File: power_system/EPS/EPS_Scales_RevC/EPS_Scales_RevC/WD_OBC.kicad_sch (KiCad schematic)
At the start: 38 parts, among them J18 Conn_01x04, J19 Conn_01x04, U14 TLV1704

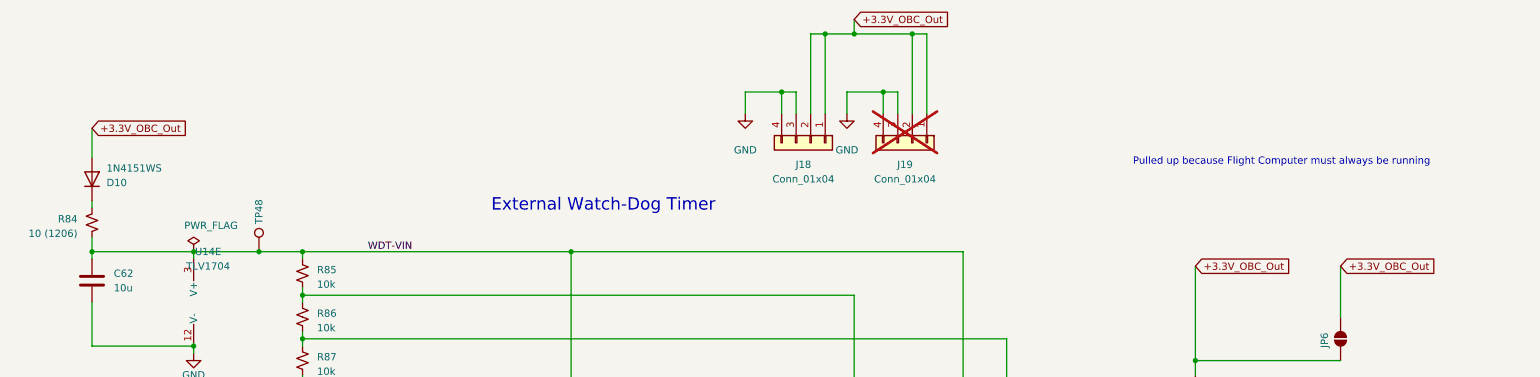
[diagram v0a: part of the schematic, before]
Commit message: Schematic and Layout changes
Made all watch dogs powered by +5v perif supply
All INAs are now powered by the 3.3v OBC supply.
DFU 16 connectors were updated to through hole versions.
Redundant test points were removed.
Layout needs work to reroute new items.
Still need to add I2C buffer
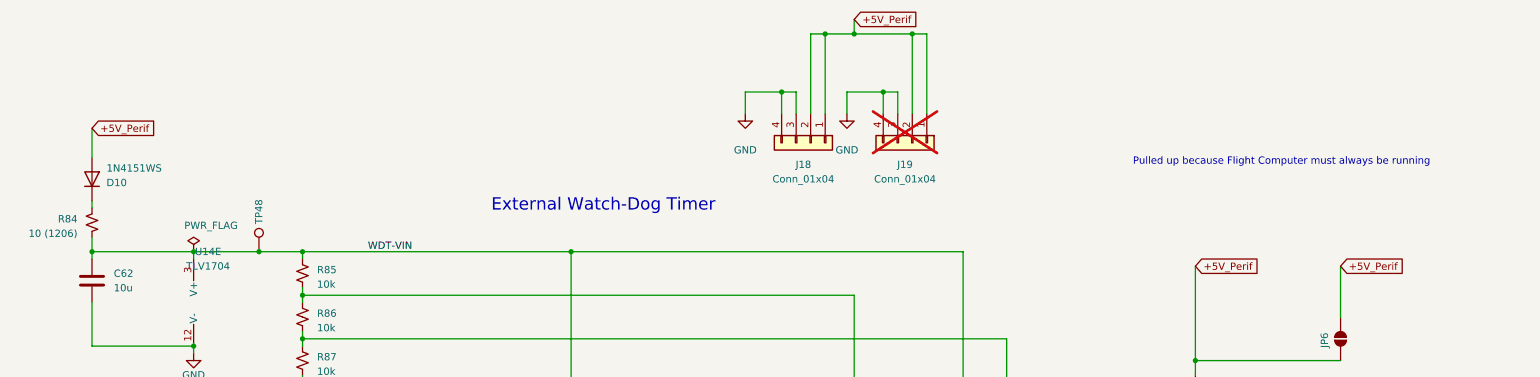
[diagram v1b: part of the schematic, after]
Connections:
- net +3.3V_OBC_Out renamed +5V_Perif
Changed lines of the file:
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@@
-		)
-	)
-	(global_label "+3.3V_OBC_Out"
-		(shape input)
-		(at 163.83 15.24 0)
-		(fields_autoplaced yes)
-		(effects
-			(font
-				(size 1.27 1.27)
-			)
-			(justify left)
-		)
-		(property "Intersheetrefs" "${INTERSHEET_REFS}"
-			(at 181.5109 15.24 0)
-			(effects
-				(font
-					(size 1.27 1.27)
-				)
-				(justify left)
-				(hide yes)
-			)
-		)
-	)
-	(global_label "+3.3V_OBC_Out"
-		(shape input)
-		(at 30.48 34.29 0)
-		(fields_autoplaced yes)
-		(effects
-			(font
-				(size 1.27 1.27)
-			)
-			(justify left)
-		)
-		(property "Intersheetrefs" "${INTERSHEET_REFS}"
-			(at 48.1609 34.29 0)
-			(effects
-				(font
-					(size 1.27 1.27)
-				)
-				(justify left)
-				(hide yes)
-			)
 		)
 	)
@@
 		)
 	)
-	(global_label "+3.3V_OBC_Out"
+	(global_label "+5V_Perif"
+		(shape input)
+		(at 163.83 15.24 0)
+		(fields_autoplaced yes)
+		(effects
+			(font
+				(size 1.27 1.27)
+			)
+			(justify left)
+		)
+		(property "Intersheetrefs" "${INTERSHEET_REFS}"
+			(at 176.1286 15.24 0)
+			(effects
+				(font
+					(size 1.27 1.27)
+				)
+				(justify left)
+				(hide yes)
+			)
+		)
+	)
+	(global_label "+5V_Perif"
 		(shape input)
 		(at 223.52 58.42 0)
@@
 		)
 		(property "Intersheetrefs" "${INTERSHEET_REFS}"
-			(at 241.2009 58.42 0)
-			(effects
-				(font
-					(size 1.27 1.27)
-				)
-				(justify left)
-				(hide yes)
-			)
-		)
-	)
-	(global_label "+3.3V_OBC_Out"
-		(shape input)
-		(at 248.92 58.42 0)
-		(fields_autoplaced yes)
-		(effects
-			(font
-				(size 1.27 1.27)
-			)
-			(justify left)
-		)
-		(property "Intersheetrefs" "${INTERSHEET_REFS}"
-			(at 266.6009 58.42 0)
+			(at 235.8186 58.42 0)
 			(effects
 				(font
@@
 				(hide yes)
 			)
+		)
+	)
+	(global_label "+5V_Perif"
+		(shape input)
+		(at 30.48 34.29 0)
+		(fields_autoplaced yes)
+		(effects
+			(font
+				(size 1.27 1.27)
+			)
+			(justify left)
+		)
+		(property "Intersheetrefs" "${INTERSHEET_REFS}"
+			(at 42.7786 34.29 0)
+			(effects
+				(font
+					(size 1.27 1.27)
+				)
+				(justify left)
+				(hide yes)
+			)
+		)
+	)
+	(global_label "+5V_Perif"
+		(shape input)
+		(at 248.92 58.42 0)
+		(fields_autoplaced yes)
+		(effects
+			(font
+				(size 1.27 1.27)
+			)
+			(justify left)
+		)
+		(property "Intersheetrefs" "${INTERSHEET_REFS}"
+			(at 261.2186 58.42 0)
+			(effects
+				(font
+					(size 1.27 1.27)
+				)
+				(justify left)
+				(hide yes)
+			)

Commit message: Schematic Revisions
Added updated block diagram
Added Individual watch dog setups for each subsystem. Resistor and Capacitor values must be modified to reflect desired time range.
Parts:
- removed J19: Conn_01x04, Connector_PinSocket_2.54mm:PinSocket_1x04_P2.54mm_Vertical, symbol Connector_Generic:Conn_01x04
- removed JP6: SolderJumper_2_Open, Jumper:SolderJumper-2_P1.3mm_Open_RoundedPad1.0x1.5mm, symbol Jumper:SolderJumper_2_Open
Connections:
- net +5V_Perif renamed +3.3V_OBC

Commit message: Layout Complete
Added I2C buffer
Found replacement inductor for 10uH
Added footprints for new components
Last thing missing is changing the solder mask sizing on most footprints to remove the errors.
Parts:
- D10, D12: footprint Diode_SMD:D_SOD-323 -> RevC Footprints:SODFL2512X100N
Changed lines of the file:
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@@
 			)
 		)
-		(property "Footprint" "Diode_SMD:D_SOD-323"
+		(property "Footprint" "RevC Footprints:SODFL2512X100N"
 			(at 177.8 137.16 0)
 			(effects
@@
 			)
 		)
-		(property "Footprint" "Diode_SMD:D_SOD-323"
+		(property "Footprint" "RevC Footprints:SODFL2512X100N"
 			(at 30.48 43.18 0)
 			(effects

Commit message: Revert "Luca branch v2"
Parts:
- added J19: Conn_01x04, Connector_PinSocket_2.54mm:PinSocket_1x04_P2.54mm_Vertical, symbol Connector_Generic:Conn_01x04
- added JP6: SolderJumper_2_Open, Jumper:SolderJumper-2_P1.3mm_Open_RoundedPad1.0x1.5mm, symbol Jumper:SolderJumper_2_Open
- D10, D12: footprint RevC Footprints:SODFL2512X100N -> Diode_SMD:D_SOD-323
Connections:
- net GND: now also J19.3 (Pin_3), J19.4 (Pin_4)
- net +3.3V_OBC renamed +5V_Perif
- net +5V_Perif: now also J19.1 (Pin_1), J19.2 (Pin_2), JP6.1 (A), JP6.2 (B)
